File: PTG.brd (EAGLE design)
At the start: 105.4 x 82.5 mm, 95 parts, among them IC1 TPS62120, IC2 PIC32MK1024MCF064-I_PT, IC3 LT1762EMS8-5PBF, IC4 TPS561208DDCR, IC5 LT1762EMS8-5PBF, J1 STX-3100-5N, J2 RCJ-01X_PHONO_SINGLE, U4 PCM1748E/2K, X1 22-23-2041, Y1 EXTERNALCRYSTAL

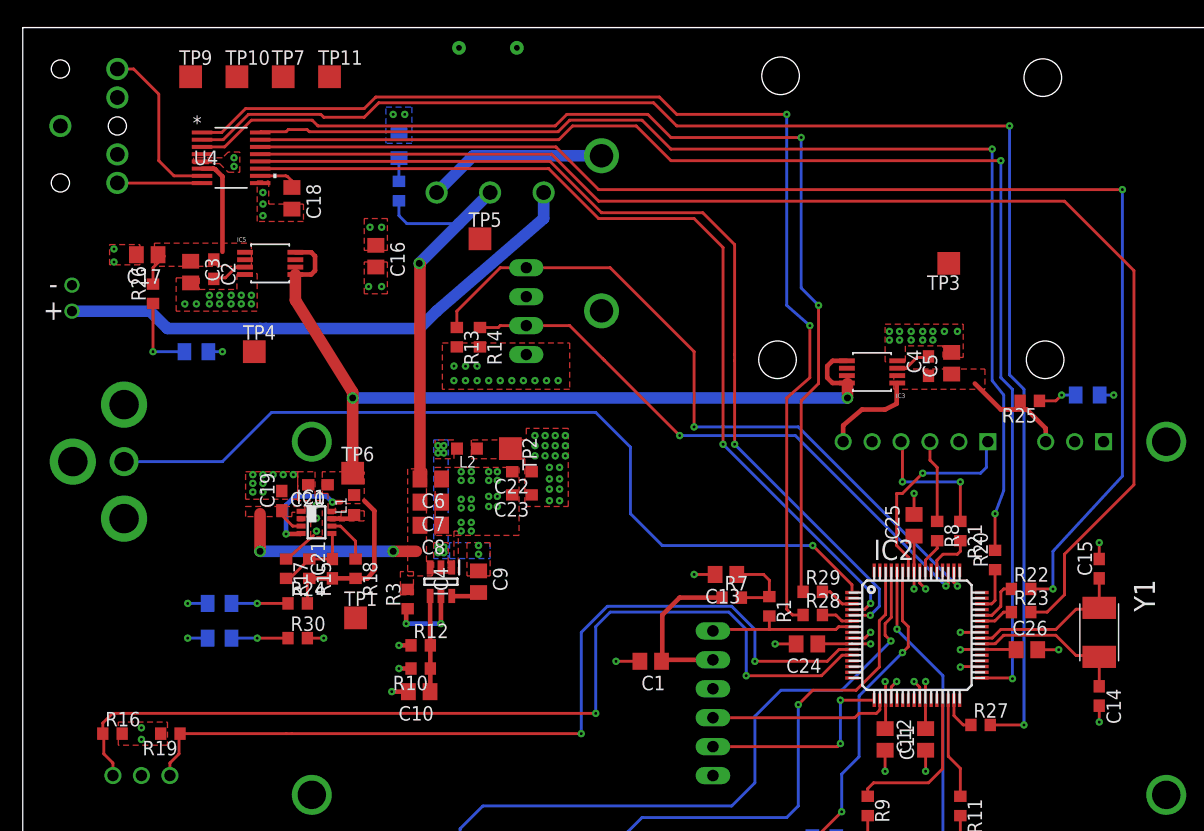
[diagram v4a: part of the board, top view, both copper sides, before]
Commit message: changes from meeting, added logos, changed test points, changed ground plane
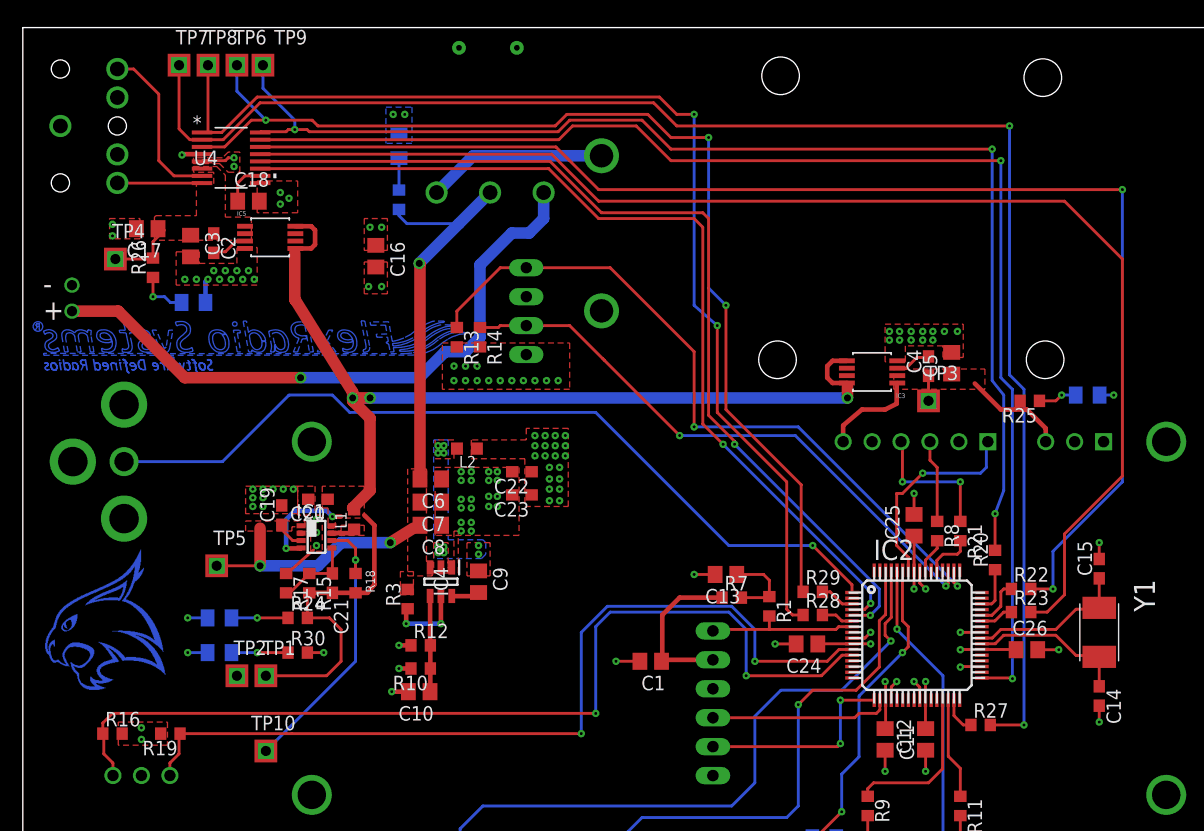
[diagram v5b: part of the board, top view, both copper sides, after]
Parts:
- removed TP11: TPTP20SQ, testpad:TP20SQ
- added TP8: TPSQTP20SQD, testpad:TP20SQD
- R31: value 365 -> (none)
- TP1, TP10, TP2, TP3, TP4, TP5, TP6, TP7, TP9: value TPTP20SQ -> TPSQTP20SQD; device testpad:TP20SQ -> testpad:TP20SQD
- moved TP10 59.2 mm to (21.3, 19.1)
- moved TP6 37.2 mm to (18.8, 79.2)
- moved TP5 36.9 mm to (17.0, 35.3)
- moved TP2 31.2 mm to (18.8, 25.7), turned to 0 degrees
- moved TP4 14.7 mm to (8.13, 62.2)
- moved TP3 12.2 mm to (79.5, 49.8), turned to 0 degrees
- moved TP1 9.37 mm to (21.3, 25.7)
- moved TP7 9.20 mm to (13.7, 79.2)
- moved TP9 6.43 mm to (21.1, 79.2)
- moved LED8 4.33 mm to (15.0, 58.4)
- moved C18 3.82 mm to (19.8, 67.3), turned to 0 degrees
- moved C17 2.29 mm to (10.9, 64.9)
- moved IC5 2.29 mm to (21.7, 64.1)
- moved C2 2.29 mm to (16.8, 63.6)
- moved R26 2.29 mm to (11.4, 61.5)
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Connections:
- net +3V3: now also TP2.1
- net +5_DAC: now also TP4.1
- net 5V_I/O: now also TP1.1, TP1.TP; no longer TP6.TP
- net AGND: now also C17.2, C3.2, IC5.4, LED8.1, U4.4
- net DAC_BCK: now also TP8.1, TP8.TP; no longer TP10.TP
- net DAC_DATA: now also TP7.1
- net DAC_LRCK: now also TP6.1, TP6.TP; no longer TP9.TP
- net GND: now also J2.1', J2.1''; no longer C17.2, C3.2, IC5.4, J2.3, J2.4, LED8.1, U4.4
- net PWRGOOD: now also TP10.1, TP10.TP; no longer TP1.TP
- net SUPPLY: now also TP5.1
- net SYS_CLK: now also TP9.1, TP9.TP; no longer TP11.TP
- net VOUT_LCD: now also TP3.1
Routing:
- net 5V_I/O: track 97.6 -> 119.3 mm, vias 4 -> 5
- net PWRGOOD: track 4.19 -> 25.8 mm, vias 0 -> 1
- net DAC_DATA: track 129.3 -> 137.1 mm
- net PWR_PIN: track 48.0 -> 55.6 mm, vias 1 -> 2
- net SYS_CLK: track 101.6 -> 108.4 mm, vias 2 -> 3
- net +5_DAC: track 11.8 -> 6.48 mm
- net SUPPLY: track 53.6 -> 57.6 mm
- net AGND: track 0.03 -> 3.95 mm, vias 3 -> 17
- net N$26: track 6.99 -> 4.41 mm
- net N$233: track 0.00 -> 2.50 mm
- net N$240: track 0.00 -> 2.47 mm
- net N$214: track 0.00 -> 2.45 mm
- net N$205: track 0.00 -> 2.41 mm
- net N$230: track 0.00 -> 2.37 mm
- net VOUT_LCD: track 18.6 -> 20.8 mm
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- added copper zone on layer 16, net FLEXR

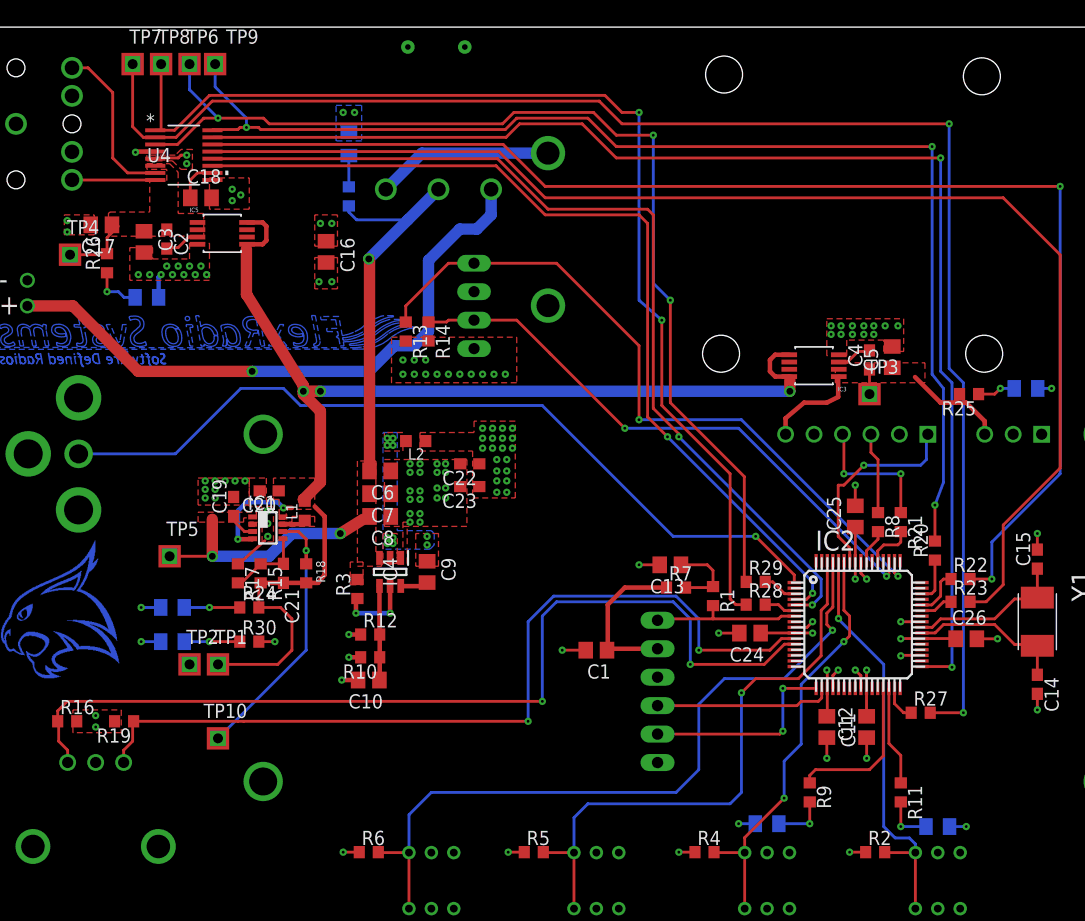
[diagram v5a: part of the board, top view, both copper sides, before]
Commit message: minor changes, added power inductor, but bad library
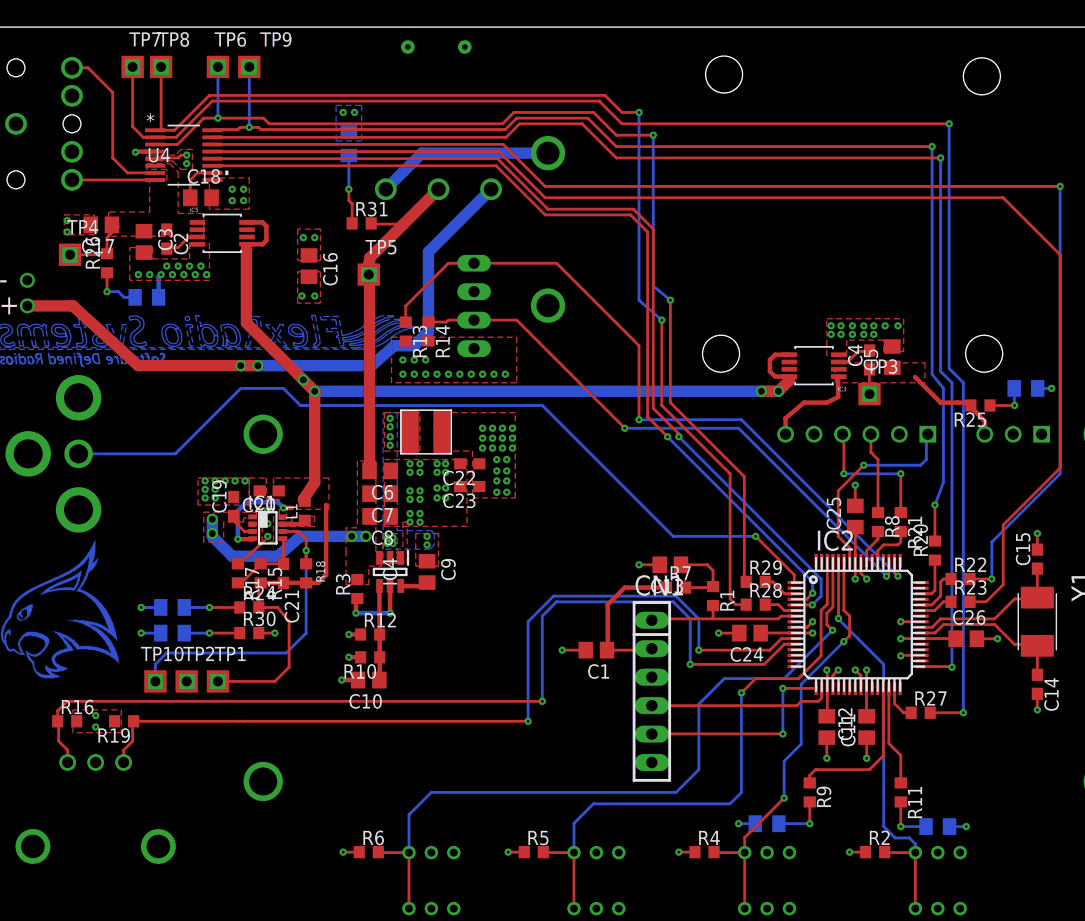
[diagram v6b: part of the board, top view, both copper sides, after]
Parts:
- L2: value 2.20uH -> 3.3uH; device NewSDR:C0603K -> PowerInductor:VLCF4020
- R10: value 3.09k -> 332k
- R12: value 10.0k -> 100k
- R24: value (none) -> 536
- R25, R26: value (none) -> 499
- R30: value (none) -> 332
- R31: value (none) -> 1.21k
- moved TP5 30.8 mm to (34.8, 60.5)
- moved TP10 7.55 mm to (15.7, 24.1)
- moved L2 3.37 mm to (42.2, 44.5), turned to 90 degrees
- moved TP9 3.06 mm to (24.1, 79.0)
- moved R31 2.67 mm to (34.2, 65.0), flipped to the top, turned to 0 degrees
- moved TP6 2.55 mm to (21.3, 79.0)
- moved C16 1.98 mm to (29.5, 61.2)
- moved TP2 1.55 mm to (18.5, 24.1)
- moved TP1 1.52 mm to (21.3, 24.1)
- moved R25 1.44 mm to (89.4, 48.8)
- moved LED9 0.76 mm to (17.3, 28.4)
- moved R30 0.76 mm to (24.1, 28.4)
- moved CN1 0.51 mm to (60.1, 23.2), flipped to the top
- moved TP7 0.25 mm to (13.7, 79.0)
- moved TP8 0.25 mm to (16.3, 79.0)
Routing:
- net SUPPLY: track 57.6 -> 50.2 mm, vias 3 -> 4
- net PWRGOOD: track 25.8 -> 29.3 mm
- net N$13: track 2.80 -> 6.18 mm, vias 0 -> 1
- net SYS_CLK: track 108.4 -> 107.0 mm
- net DAC_LRCK: track 96.1 -> 94.9 mm
- net 5V_I/O: track 119.3 -> 120.1 mm, vias 5 -> 6
- net DAC_ZEROL: track 84.4 -> 83.7 mm
- net N$16: track 18.1 -> 18.7 mm
- net N$25: track 15.8 -> 16.3 mm
- net !MCLR: track 13.5 -> 14.0 mm
- net PWR_PIN: vias 2 -> 3
- net AGND: vias 17 -> 18

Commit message: arracnged silk screen layer
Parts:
- moved LED4 1.52 mm to (17.3, 32.3)
- moved LED1 0.25 mm to (85.6, 11.4)
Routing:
- net DAC_LRCK: track 94.9 -> 95.7 mm
- net DAC_BCK: track 99.3 -> 99.8 mm
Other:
- board text added: "1 kHz = On"
- board text added: "3.3V SW Out"
- board text added: "3v3"
- board text added: "5V"
- board text added: "5V SW Out"
- board text added: "BCK"
- board text added: "DAC LDO Out"
- board text added: "DATA"
- board text added: "Freq Step"
- board text added: "LDO"
- board text added: "LR"
- board text added: "Line / Mic"
- board text added: "Line = On"
- board text added: "PG"
- board text added: "SYS"
- board text added: "Supply"

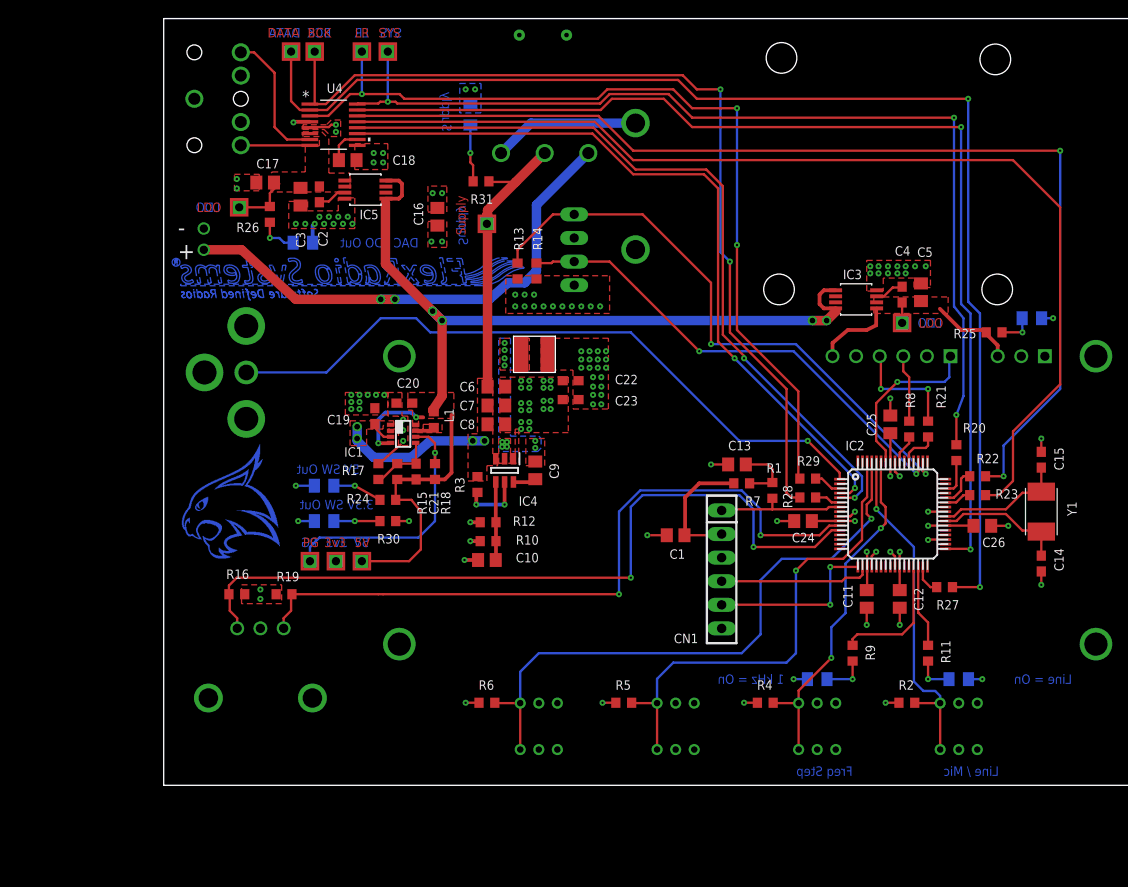
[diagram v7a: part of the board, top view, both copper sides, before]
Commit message: Fixed library symbols for chassis grounds, renamed voltage nodes, switched pins on molex power conn, updated power inductors, updated through hole RCA port
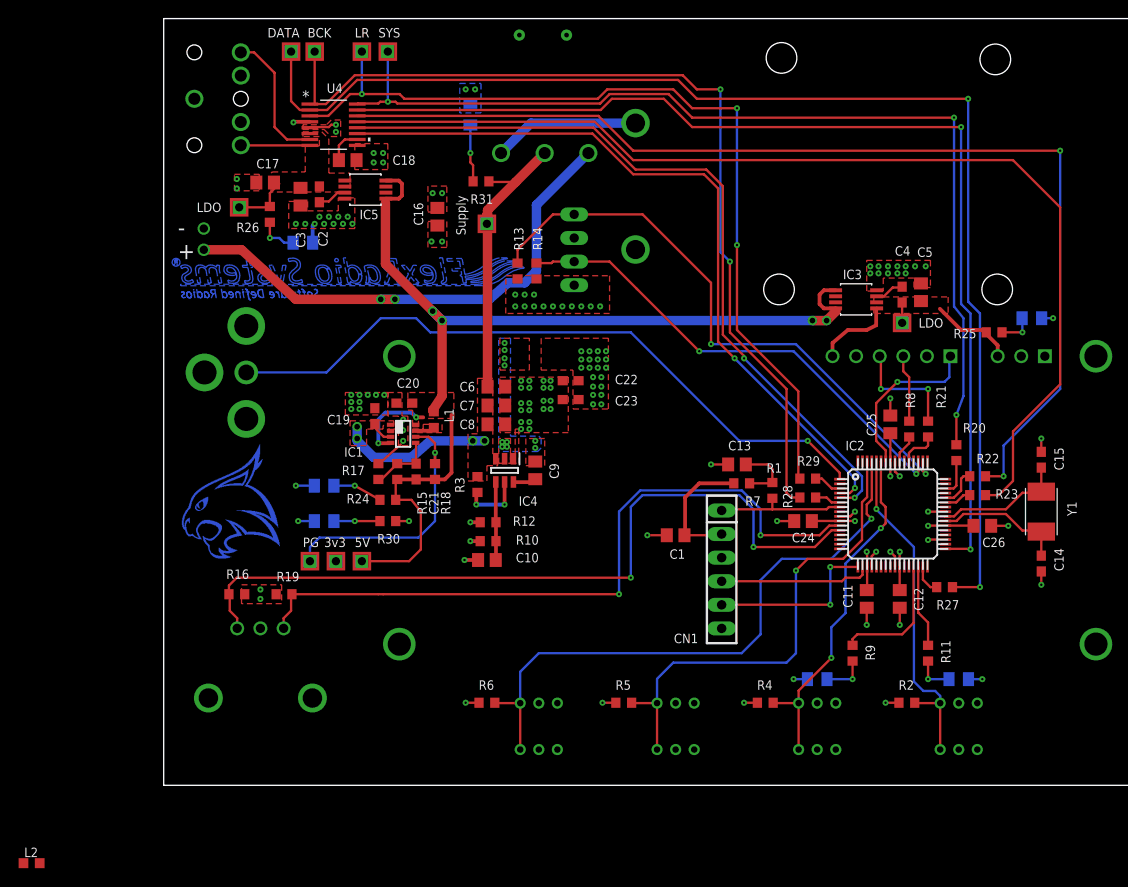
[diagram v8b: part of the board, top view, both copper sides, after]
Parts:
- L2: device PowerInductor:VLCF4020 -> NewSDR:C0603K
- R10: value 332k -> 33.2k
- R12: value 100k -> 10.0k
- moved L2 77.3 mm to (-14.2, -8.38), turned to 0 degrees
